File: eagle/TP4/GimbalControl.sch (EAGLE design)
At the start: 6 parts, among them M1 SERVO, M2 SERVO

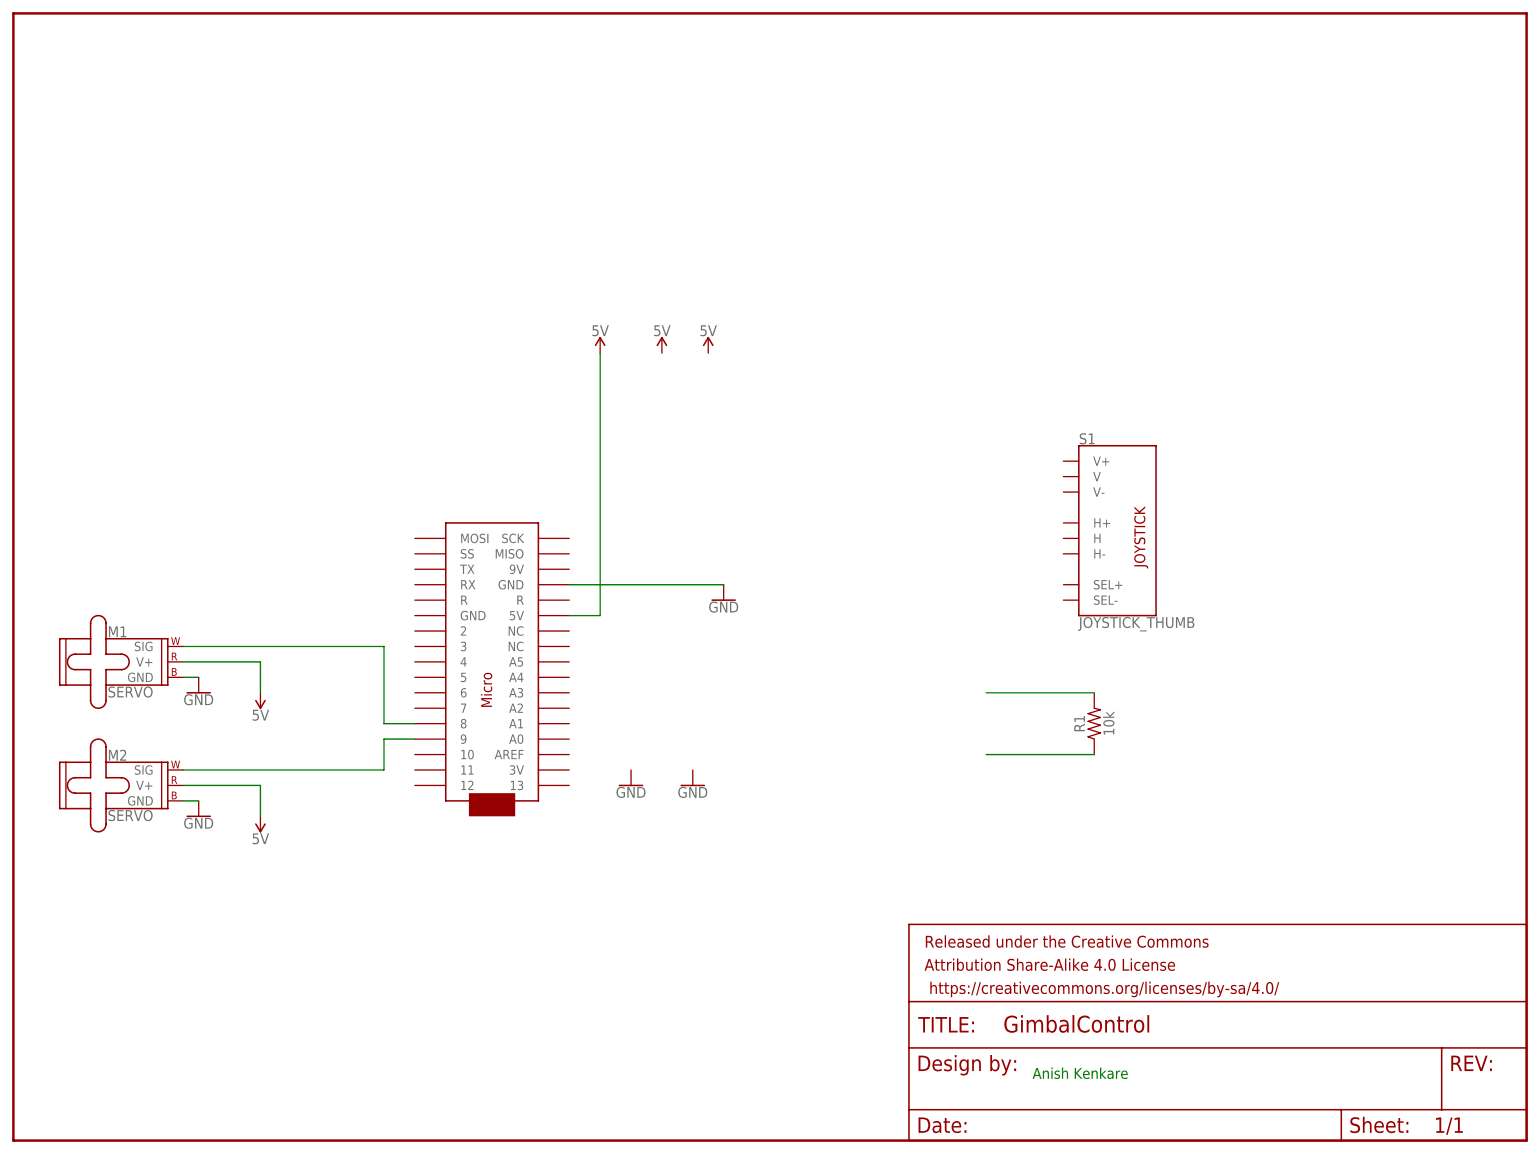
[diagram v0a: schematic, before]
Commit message: Completed PCB for Gimbal Control
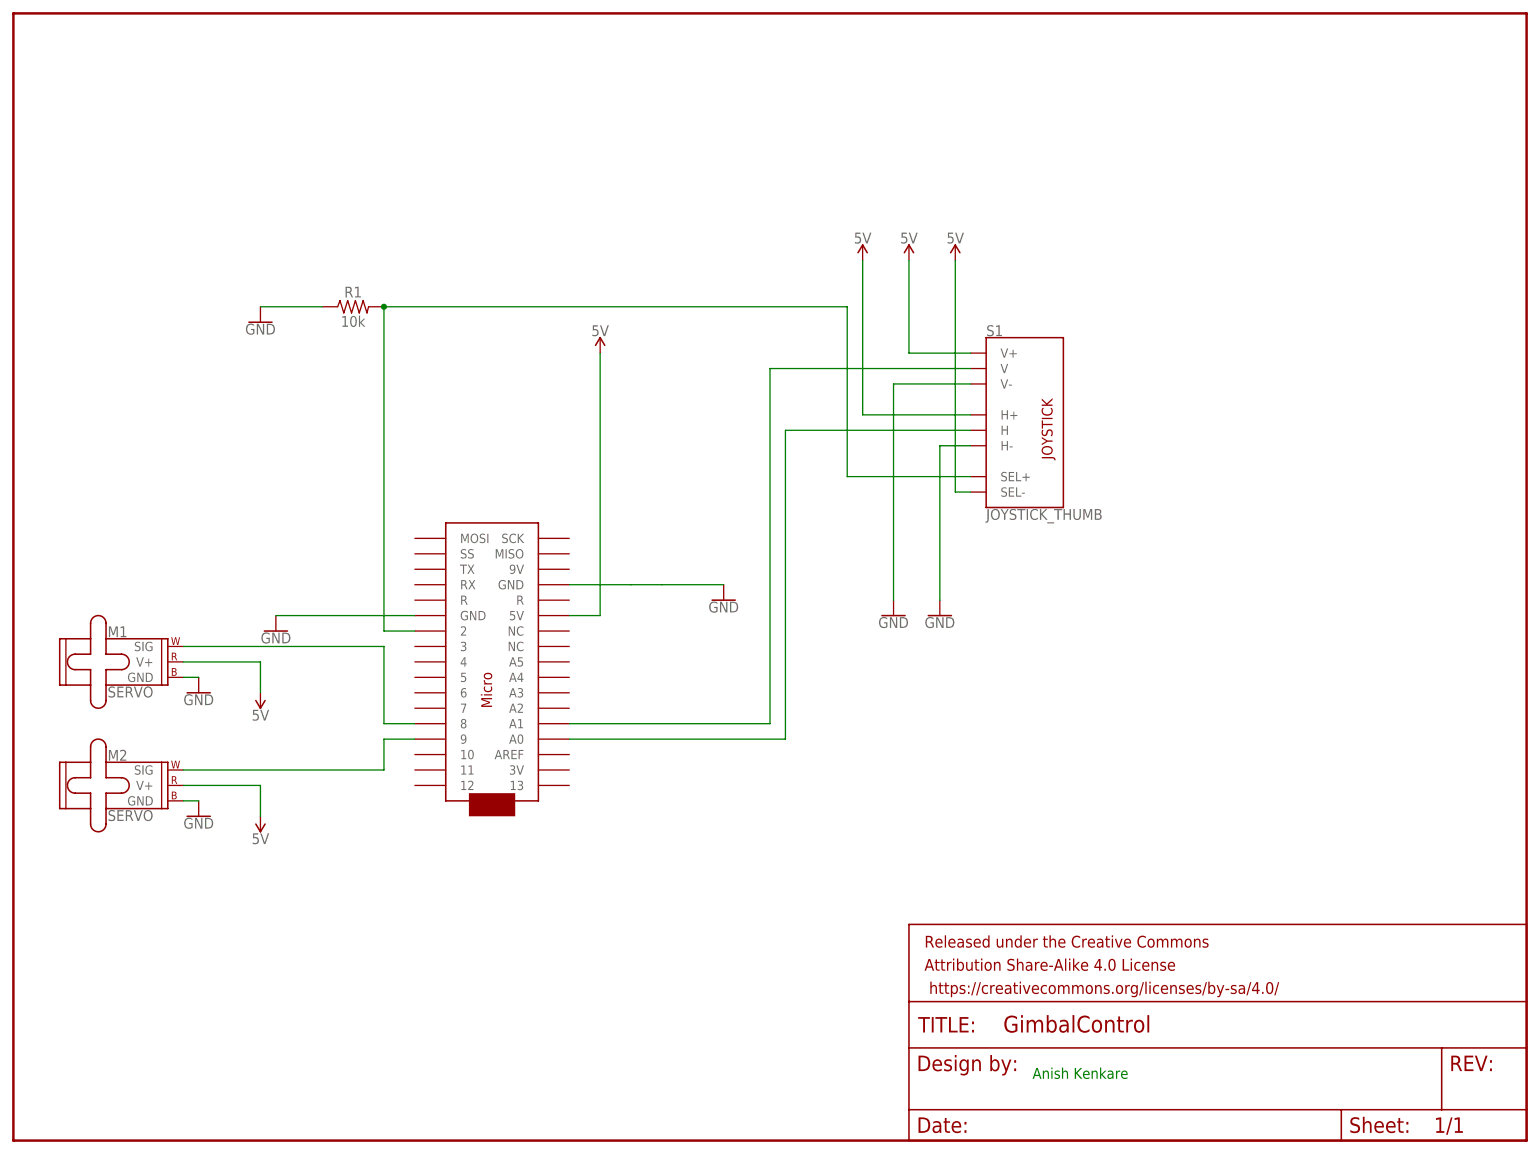
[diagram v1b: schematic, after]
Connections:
- removed net N$2: R1.1
- new net N$5: S1.V, U$1.A1
- new net N$6: S1.H, U$1.A0
- net 5V: now also S1.H+, S1.SEL-, S1.V+
- net GND: now also R1.1, S1.H-, S1.V-, U$1.GND@1
- net N$1: now also S1.SEL+, U$1.2
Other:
- moved on the sheet: R1, S1
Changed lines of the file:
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@@
 <part name="SUPPLY5" library="SparkFun-PowerSymbols" library_urn="urn:adsk.eagle:library:530" deviceset="5V" device=""/>
 <part name="GND5" library="SparkFun-PowerSymbols" library_urn="urn:adsk.eagle:library:530" deviceset="GND" device=""/>
+<part name="GND6" library="SparkFun-PowerSymbols" library_urn="urn:adsk.eagle:library:530" deviceset="GND" device=""/>
+<part name="GND8" library="SparkFun-PowerSymbols" library_urn="urn:adsk.eagle:library:530" deviceset="GND" device=""/>
+<part name="SUPPLY6" library="SparkFun-PowerSymbols" library_urn="urn:adsk.eagle:library:530" deviceset="5V" device=""/>
 </parts>
 <sheets>
@@
 <instance part="FRAME1" gate="G$1" x="0" y="0"/>
 <instance part="FRAME1" gate="V" x="147.32" y="0"/>
-<instance part="S1" gate="G$1" x="182.88" y="101.6"/>
-<instance part="R1" gate="G$1" x="177.8" y="68.58" rot="R90"/>
+<instance part="S1" gate="G$1" x="167.64" y="119.38"/>
+<instance part="R1" gate="G$1" x="55.88" y="137.16"/>
 <instance part="M1" gate="G$1" x="25.4" y="81.28"/>
 <instance part="M2" gate="G$1" x="25.4" y="60.96"/>
 <instance part="GND1" gate="1" x="116.84" y="88.9"/>
-<instance part="GND2" gate="1" x="101.6" y="58.42"/>
+<instance part="GND2" gate="1" x="43.18" y="83.82"/>
 <instance part="GND3" gate="1" x="30.48" y="73.66"/>
 <instance part="GND4" gate="1" x="30.48" y="53.34"/>
@@
 <instance part="SUPPLY2" gate="G$1" x="40.64" y="53.34" rot="R180"/>
 <instance part="SUPPLY3" gate="G$1" x="96.52" y="129.54"/>
-<instance part="SUPPLY4" gate="G$1" x="106.68" y="129.54"/>
-<instance part="SUPPLY5" gate="G$1" x="114.3" y="129.54"/>
-<instance part="GND5" gate="1" x="111.76" y="58.42"/>
+<instance part="SUPPLY4" gate="G$1" x="139.7" y="144.78"/>
+<instance part="SUPPLY5" gate="G$1" x="147.32" y="144.78"/>
+<instance part="GND5" gate="1" x="144.78" y="86.36"/>
+<instance part="GND6" gate="1" x="152.4" y="86.36"/>
+<instance part="GND8" gate="1" x="40.64" y="134.62"/>
+<instance part="SUPPLY6" gate="G$1" x="154.94" y="144.78"/>
 </instances>
 <busses>
@@
 <segment>
 <pinref part="R1" gate="G$1" pin="2"/>
-<wire x1="160.02" y1="73.66" x2="177.8" y2="73.66" width="0.1524" layer="91"/>
-</segment>
-</net>
-<net name="N$2" class="0">
-<segment>
-<pinref part="R1" gate="G$1" pin="1"/>
-<wire x1="160.02" y1="63.5" x2="177.8" y2="63.5" width="0.1524" layer="91"/>
+<pinref part="U$1" gate="G$1" pin="2"/>
+<wire x1="60.96" y1="137.16" x2="60.96" y2="83.82" width="0.1524" layer="91"/>
+<wire x1="60.96" y1="83.82" x2="66.04" y2="83.82" width="0.1524" layer="91"/>
+<wire x1="60.96" y1="137.16" x2="137.16" y2="137.16" width="0.1524" layer="91"/>
+<junction x="60.96" y="137.16"/>
+<wire x1="137.16" y1="137.16" x2="137.16" y2="109.22" width="0.1524" layer="91"/>
+<pinref part="S1" gate="G$1" pin="SEL+"/>
+<wire x1="137.16" y1="109.22" x2="157.48" y2="109.22" width="0.1524" layer="91"/>
 </segment>
 </net>
@@
 <wire x1="27.94" y1="55.88" x2="30.48" y2="55.88" width="0.1524" layer="91"/>
 <pinref part="GND4" gate="1" pin="GND"/>
+</segment>
+<segment>
+<pinref part="GND2" gate="1" pin="GND"/>
+<pinref part="U$1" gate="G$1" pin="GND@1"/>
+<wire x1="43.18" y1="86.36" x2="66.04" y2="86.36" width="0.1524" layer="91"/>
+</segment>
+<segment>
+<pinref part="S1" gate="G$1" pin="V-"/>
+<wire x1="157.48" y1="124.46" x2="144.78" y2="124.46" width="0.1524" layer="91"/>
+<pinref part="GND5" gate="1" pin="GND"/>
+<wire x1="144.78" y1="124.46" x2="144.78" y2="88.9" width="0.1524" layer="91"/>
+</segment>
+<segment>
+<pinref part="S1" gate="G$1" pin="H-"/>
+<pinref part="GND6" gate="1" pin="GND"/>
+<wire x1="157.48" y1="114.3" x2="152.4" y2="114.3" width="0.1524" layer="91"/>
+<wire x1="152.4" y1="114.3" x2="152.4" y2="88.9" width="0.1524" layer="91"/>
+</segment>
+<segment>
+<pinref part="R1" gate="G$1" pin="1"/>
+<wire x1="40.64" y1="137.16" x2="50.8" y2="137.16" width="0.1524" layer="91"/>
+<pinref part="GND8" gate="1" pin="GND"/>
 </segment>
 </net>
@@
 <wire x1="96.52" y1="86.36" x2="91.44" y2="86.36" width="0.1524" layer="91"/>
 </segment>
+<segment>
+<pinref part="SUPPLY5" gate="G$1" pin="5V"/>
+<wire x1="147.32" y1="144.78" x2="147.32" y2="129.54" width="0.1524" layer="91"/>
+<pinref part="S1" gate="G$1" pin="V+"/>
+<wire x1="147.32" y1="129.54" x2="157.48" y2="129.54" width="0.1524" layer="91"/>
+</segment>
+<segment>
+<pinref part="SUPPLY4" gate="G$1" pin="5V"/>
+<pinref part="S1" gate="G$1" pin="H+"/>
+<wire x1="139.7" y1="144.78" x2="139.7" y2="119.38" width="0.1524" layer="91"/>
+<wire x1="139.7" y1="119.38" x2="157.48" y2="119.38" width="0.1524" layer="91"/>
+</segment>
+<segment>
+<pinref part="S1" gate="G$1" pin="SEL-"/>
+<wire x1="157.48" y1="106.68" x2="154.94" y2="106.68" width="0.1524" layer="91"/>
+<wire x1="154.94" y1="106.68" x2="154.94" y2="144.78" width="0.1524" layer="91"/>
+<pinref part="SUPPLY6" gate="G$1" pin="5V"/>
+</segment>
 </net>
+<net name="N$5" class="0">
+<segment>
+<pinref part="S1" gate="G$1" pin="V"/>
+<wire x1="157.48" y1="127" x2="124.46" y2="127" width="0.1524" layer="91"/>
+<wire x1="124.46" y1="127" x2="124.46" y2="68.58" width="0.1524" layer="91"/>
+<pinref part="U$1" gate="G$1" pin="A1"/>
+<wire x1="124.46" y1="68.58" x2="91.44" y2="68.58" width="0.1524" layer="91"/>
+</segment>
+</net>
+<net name="N$6" class="0">
+<segment>
+<pinref part="S1" gate="G$1" pin="H"/>
+<wire x1="157.48" y1="116.84" x2="127" y2="116.84" width="0.1524" layer="91"/>
+<wire x1="127" y1="116.84" x2="127" y2="66.04" width="0.1524" layer="91"/>
+<pinref part="U$1" gate="G$1" pin="A0"/>
+<wire x1="127" y1="66.04" x2="91.44" y2="66.04" width="0.1524" layer="91"/>
+</segment>
+</net>
